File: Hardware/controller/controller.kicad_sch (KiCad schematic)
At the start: 48 parts, among them J101 Conn_02x10_Odd_Even, J102 Conn_02x10_Odd_Even, J103 Conn_02x10_Odd_Even, J104 Conn_02x08_Odd_Even, M101 Fan_4pin, Q101 MMBT3904, U101 PCA9543A, U102 EMC2101-R

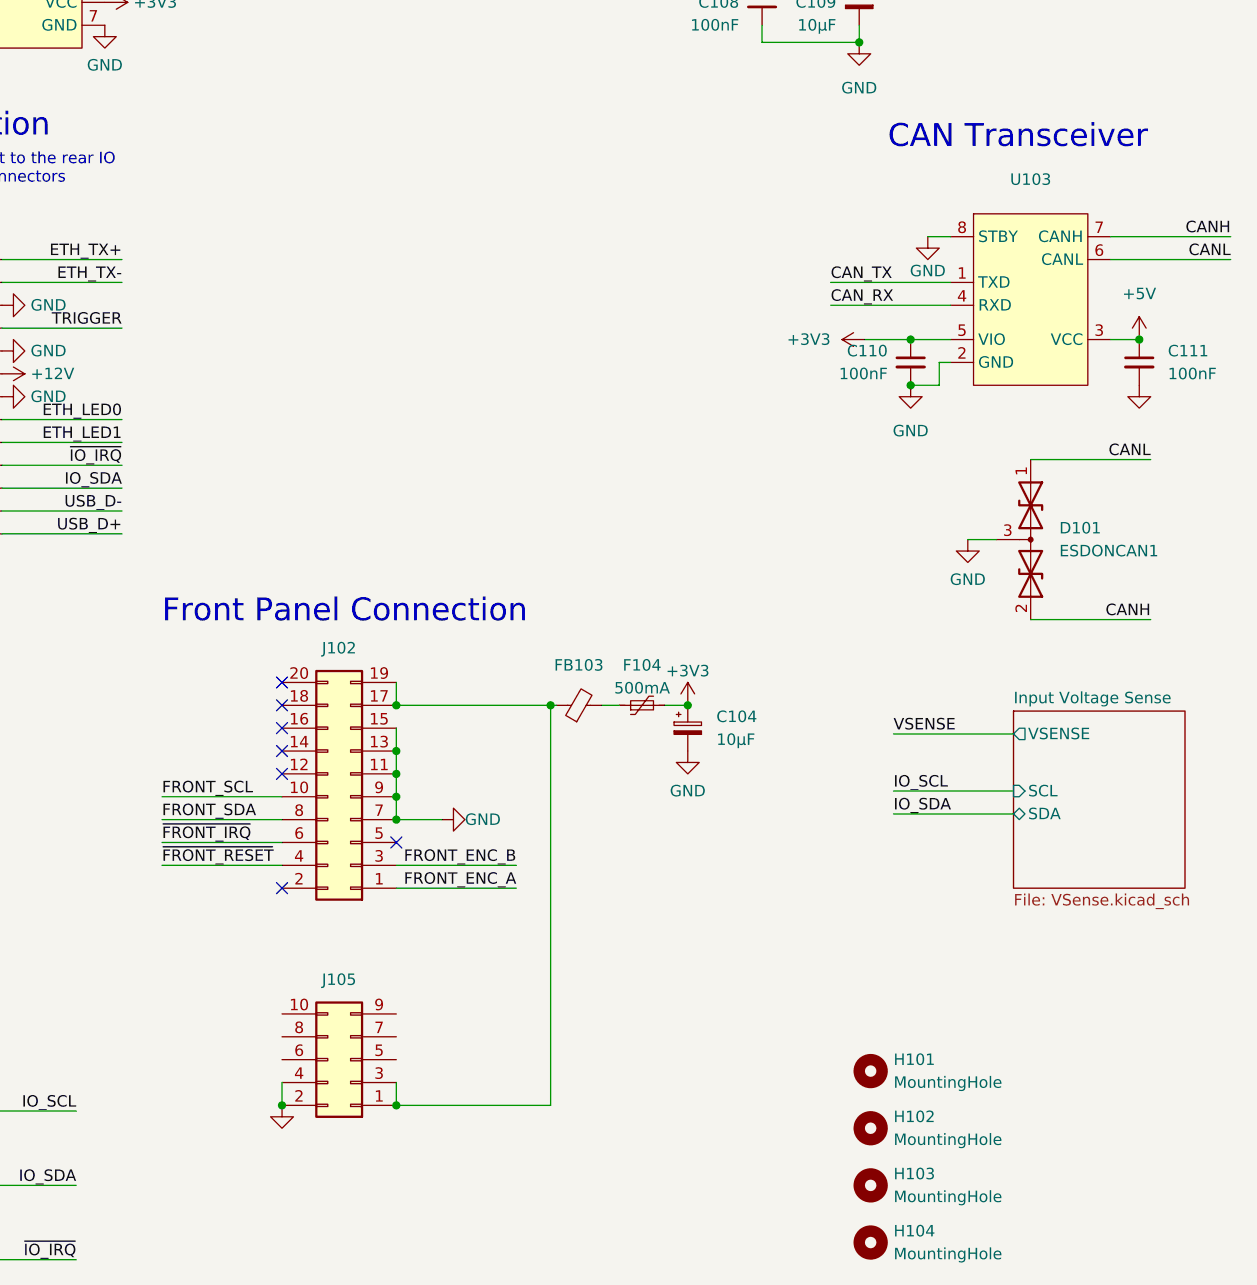
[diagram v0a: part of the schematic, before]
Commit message: Add "bonus display" board
- Created the bonus display board, which houses a chip-on-glass 4x10
  text character display. It's meant to be mounted next to the input
  jacks to show a constant location of current/voltage, even if the main
  display is used for menus or other stuff.

- More tweaks to controller board, to do with power generation and the
  front panel bonus display connector
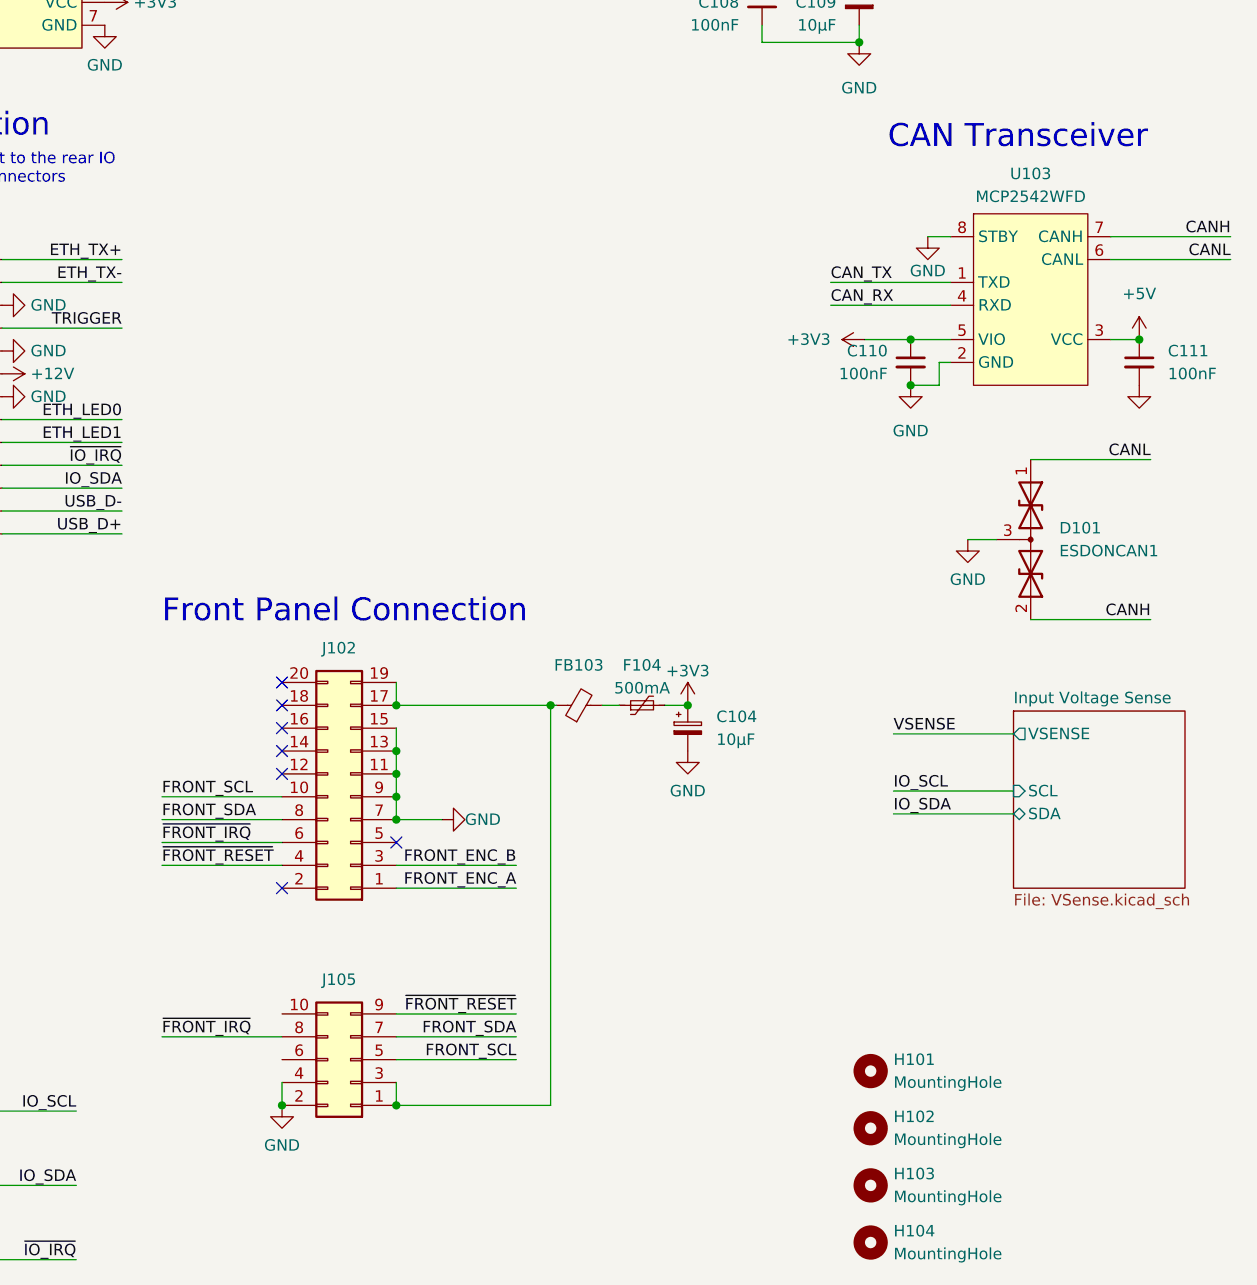
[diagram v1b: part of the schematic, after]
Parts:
- J105: value (none) -> Conn_02x05_Odd_Even; footprint (none) -> Connector_PinHeader_1.27mm:PinHeader_2x05_P1.27mm_Vertical_SMD
- U103: value (none) -> MCP2542WFD; footprint (none) -> Package_SO:SOIC-8_3.9x4.9mm_P1.27mm
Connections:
- net FRONT_SCL: now also J105.5 (Pin_5)
- net FRONT_SDA: now also J105.7 (Pin_7)
- net ~{FRONT_IRQ}: now also J105.8 (Pin_8)
- net ~{FRONT_RESET}: now also J105.9 (Pin_9)
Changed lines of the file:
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@@
+    (stroke (width 0) (type default) (color 0 0 0 0))
+  )
+  (wire (pts (xy 116.205 166.37) (xy 102.87 166.37))
     (stroke (width 0) (type default) (color 0 0 0 0))
   )
@@
     (stroke (width 0) (type default) (color 0 0 0 0))
   )
+  (wire (pts (xy 116.205 171.45) (xy 102.87 171.45))
+    (stroke (width 0) (type default) (color 0 0 0 0))
+  )
   (wire (pts (xy 186.69 104.775) (xy 173.355 104.775))
     (stroke (width 0) (type default) (color 0 0 0 0))
@@
     (stroke (width 0) (type default) (color 0 0 0 0))
   )
+  (wire (pts (xy 116.205 168.91) (xy 102.87 168.91))
+    (stroke (width 0) (type default) (color 0 0 0 0))
+  )
   (wire (pts (xy 76.835 147.32) (xy 90.17 147.32))
     (stroke (width 0) (type default) (color 0 0 0 0))
@@
   )
   (wire (pts (xy 46.355 185.42) (xy 46.355 177.165))
+    (stroke (width 0) (type default) (color 0 0 0 0))
+  )
+  (wire (pts (xy 76.835 168.91) (xy 90.17 168.91))
     (stroke (width 0) (type default) (color 0 0 0 0))
   )
@@
     (effects (font (size 1.27 1.27)) (justify left bottom))
   )
+  (label "FRONT_SDA" (at 116.205 168.91 180)
+    (effects (font (size 1.27 1.27)) (justify right bottom))
+  )
   (label "CAN_TX" (at 151.13 85.09 0)
     (effects (font (size 1.27 1.27)) (justify left bottom))
@@
     (effects (font (size 1.27 1.27)) (justify right bottom))
   )
+  (label "FRONT_SCL" (at 116.205 171.45 180)
+    (effects (font (size 1.27 1.27)) (justify right bottom))
+  )
   (label "ETH_TX+" (at 208.915 88.265 0)
     (effects (font (size 1.27 1.27)) (justify left bottom))
@@
     (effects (font (size 1.27 1.27)) (justify left bottom))
   )
+  (label "~{FRONT_IRQ}" (at 76.835 168.91 0)
+    (effects (font (size 1.27 1.27)) (justify left bottom))
+  )
   (label "IO_SCL" (at 67.31 177.165 180)
     (effects (font (size 1.27 1.27)) (justify right bottom))
@@
   (label "VSENSE" (at 208.915 114.935 0)
     (effects (font (size 1.27 1.27)) (justify left bottom))
+  )
+  (label "~{FRONT_RESET}" (at 116.205 166.37 180)
+    (effects (font (size 1.27 1.27)) (justify right bottom))
   )
   (symbol (lib_id "Device:D_TVS_Dual_AAC") (at 173.355 113.665 270) (unit 1)
@@
       (effects (font (size 1.27 1.27)) hide)
     )
-    (property "Value" "" (id 1) (at 90.17 180.975 0))
+    (property "Value" "GND" (id 1) (at 90.17 180.975 0))
     (property "Footprint" "" (id 2) (at 90.17 176.53 0)
       (effects (font (size 1.27 1.27)) hide)
@@
   (symbol (lib_id "programmable-load:MCP2542WFD") (at 173.355 85.09 0) (unit 1)
     (in_bom yes) (on_board yes)
-    (property "Reference" "U103" (id 0) (at 173.355 73.66 0))
-    (property "Value" "" (id 1) (at 173.355 76.2 0))
-    (property "Footprint" "" (id 2) (at 173.355 97.79 0)
+    (property "Reference" "U103" (id 0) (at 173.355 73.025 0))
+    (property "Value" "MCP2542WFD" (id 1) (at 173.355 75.565 0))
+    (property "Footprint" "Package_SO:SOIC-8_3.9x4.9mm_P1.27mm" (id 2) (at 173.355 97.79 0)
       (effects (font (size 1.27 1.27) italic) hide)
     )
@@
     (in_bom yes) (on_board yes)
     (property "Reference" "J105" (id 0) (at 96.52 162.56 0))
-    (property "Value" "" (id 1) (at 96.52 161.925 0)
-      (effects (font (size 1.27 1.27)) hide)
-    )
-    (property "Footprint" "" (id 2) (at 97.79 171.45 0)
-      (effects (font (size 1.27 1.27)) hide)
-    )
+    (property "Value" "Conn_02x05_Odd_Even" (id 1) (at 96.52 161.925 0)
+      (effects (font (size 1.27 1.27)) hide)
+    )
+    (property "Footprint" "Connector_PinHeader_1.27mm:PinHeader_2x05_P1.27mm_Vertical_SMD" (id 2) (at 97.79 171.45 0)
+      (effects (font (size 1.27 1.27)) hide)
+    )

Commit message: Refactoring controller schematic
- Moved most of the connections out of the main sheet and into
  appropriate subsheets to increase the organization

- Updated analog board connection to have the SPI bus concept rather
  than a CAN bus; that way we don't need an additional micro on the
  analog board to drive things also

- Replaced latching connectors with regular shrouded headers
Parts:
- removed C103, C104, C109: 10µF, Capacitor_Tantalum_SMD:CP_EIA-3216-18_Kemet-A_Pad1.58x1.35mm_HandSolder, symbol Device:C_Polarized_Small
- removed C106, C108, C110, C111: 100nF, Capacitor_SMD:C_0805_2012Metric_Pad1.18x1.45mm_HandSolder, symbol Device:C_Small
- removed D101: ESDONCAN1, Package_TO_SOT_SMD:SOT-23_Handsoldering, symbol Device:D_TVS_Dual_AAC
- removed F103: 250mA, Fuse:Fuse_1206_3216Metric_Pad1.42x1.75mm_HandSolder, symbol Device:Polyfuse_Small
- removed F104, F105: 500mA, Fuse:Fuse_1206_3216Metric_Pad1.42x1.75mm_HandSolder, symbol Device:Polyfuse_Small
- removed FB101, FB103: FerriteBead_Small, Inductor_SMD:L_0805_2012Metric_Pad1.05x1.20mm_HandSolder, symbol Device:FerriteBead_Small
- removed J102: Conn_02x10_Odd_Even, Connector_PinHeader_1.27mm:PinHeader_2x10_P1.27mm_Vertical_SMD, symbol Connector_Generic:Conn_02x10_Odd_Even
- removed J103: Conn_02x10_Odd_Even, Connector_PinHeader_1.27mm:PinHeader_2x13_P1.27mm_Vertical, symbol Connector_Generic:Conn_02x13_Odd_Even
- removed J104: Conn_02x08_Odd_Even, Connector_IDC:IDC-Header_2x08-1MP_P2.54mm_Latch_Horizontal, symbol Connector_Generic:Conn_02x08_Odd_Even
- removed J105: Conn_02x05_Odd_Even, Connector_PinHeader_1.27mm:PinHeader_2x05_P1.27mm_Vertical_SMD, symbol Connector_Generic:Conn_02x05_Odd_Even
- removed R103, R104, R105, R106: 2k2, Resistor_SMD:R_0805_2012Metric_Pad1.20x1.40mm_HandSolder, symbol Device:R_Small
- removed R107, R108, R109, R111, R112: 10k, Resistor_SMD:R_0805_2012Metric_Pad1.20x1.40mm_HandSolder, symbol Device:R_Small
- removed U102: EMC2101-R, Package_SO:MSOP-8_3x3mm_P0.65mm, symbol programmable-load:EMC2101-R
- removed U103: MCP2542WFD, Package_SO:SOIC-8_3.9x4.9mm_P1.27mm, symbol programmable-load:MCP2542WFD
- J101: footprint Connector_IDC:IDC-Header_2x05-1MP_P2.54mm_Latch_Horizontal -> Connector_IDC:IDC-Header_2x10_P2.54mm_Horizontal; symbol Connector_Generic:Conn_02x05_Odd_Even -> Connector_Generic:Conn_02x10_Odd_Even; MPN 61201022121 -> 61202021721
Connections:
- net +3V3: now also J101.13 (Pin_13), J101.15 (Pin_15)
- net GND: now also J101.7 (Pin_7); no longer J101.10 (Pin_10), J101.2 (Pin_2), J101.4 (Pin_4), J101.6 (Pin_6), J101.8 (Pin_8)
- net CANH renamed ANA_MISO
- net CANL renamed ANA_SEL0
- new net: J101.14 (Pin_14), J101.16 (Pin_16), J101.18 (Pin_18), J101.20 (Pin_20)
- new net: FB102.1, J101.17 (Pin_17), J101.19 (Pin_19)
- new net ANA_MOSI: J101.6 (Pin_6)
- new net ANA_SCK: J101.5 (Pin_5)
- new net ANA_SEL1: J101.2 (Pin_2)
- new net ~{ANA_CS}: J101.4 (Pin_4)
- new net ~{ANA_IRQ}: J101.8 (Pin_8)
- new net ~{ANA_RESET}: J101.9 (Pin_9)
- no-connect marks 11 -> 0
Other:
- added sheet Front Panel Connections (io-front.kicad_sch)
- added sheet Rear IO Connections (io-rear.kicad_sch)
- sheet CPU ports: added ANALOG_MISO, ANALOG_MOSI, ANALOG_SCK, ANALOG_SEL0, ANALOG_SEL1, FAN_PWM, ~{ANALOG_CS}, ~{ANALOG_IRQ}, ~{ANALOG_RESET}; removed ~{DRIVER_IRQ}, ~{DRIVER_RESET}
- note added: "*** TODO: fuse for +3V3"
- note added: "Analog Board Connection"
- note added: "Connect to internal load boards Provides to loads: +12V, +3V3"
- note removed: "CAN Transceiver"
- note removed: "Connect to internal load boards Provides to loads: +12V, +5V, +3V3"
- note removed: "Driver Board Connection"
- note removed: "Front Panel Connection"
- note removed: "Host loads regs, fan at 0%"
- note removed: "I²C address: 0b1001100"
- note removed: "Provide USB, I²C, CAN, Ethernet to the rear IO board, which has the actual connectors"
- note removed: "Rear IO connection"
- note removed: "To OLED"
- moved on the sheet: C101, C102, F101, FB102, R117, R118, U101

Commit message: More tweaks to controller layout
- Wired up the fan connector to work with PWM control, directly from one
  of the processor's timer/counter's signal generator outputs. For now
  the tachometer output is ignored, but we might do something with it
  later

- Moved around a few passives
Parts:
- removed C107: 10µF, Capacitor_THT:CP_Radial_D5.0mm_P2.00mm, symbol Device:C_Polarized_Small
- removed M101: Fan_4pin, programmable-load:Molex-47053-1000-MFG, symbol Motor:Fan_4pin
- removed Q101: MMBT3904, Package_TO_SOT_SMD:SOT-323_SC-70_Handsoldering, symbol Transistor_BJT:MMBT3904
- removed R113, R116: 4k7, Resistor_SMD:R_0805_2012Metric_Pad1.20x1.40mm_HandSolder, symbol Device:R_Small
- removed R114: 10k, Resistor_SMD:R_0805_2012Metric_Pad1.20x1.40mm_HandSolder, symbol Device:R_Small
- removed R115: 27k4, Resistor_SMD:R_0805_2012Metric_Pad1.20x1.40mm_HandSolder, symbol Device:R_Small
- added F102: 500mA, Fuse:Fuse_1206_3216Metric_Pad1.42x1.75mm_HandSolder, symbol Device:Polyfuse_Small
- added R101, R102: 2k2, Resistor_SMD:R_0805_2012Metric_Pad1.20x1.40mm_HandSolder, symbol Device:R_Small
- added R103: (no value), symbol Device:R_Small
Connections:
- net +3V3: now also F102.1, R101.2, R102.2, R103.2; no longer J101.13 (Pin_13), J101.15 (Pin_15)
- net ANA_SCL: now also J101.11 (Pin_11), R101.1
- net ANA_SDA: now also J101.10 (Pin_10), R102.1
- net GND: now also J101.13 (Pin_13), J101.15 (Pin_15), J101.18 (Pin_18), J101.20 (Pin_20)
- net ~{ANA_IRQ}: now also R103.1
- net at J101.14 (Pin_14), J101.16 (Pin_16): now also F102.2; no longer J101.18 (Pin_18), J101.20 (Pin_20)
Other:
- sheet CPU ports: added ANALOG_SCL, ANALOG_SDA; removed DRIVER_SCL, DRIVER_SDA
- sheet Rear IO Connections ports: added FAN_PWM; removed none
- note removed: "A 4-pin PWM fan mounted to the rear panel of the case is used to exhaust hot air"
- note removed: "Rear Panel Fan Controller"

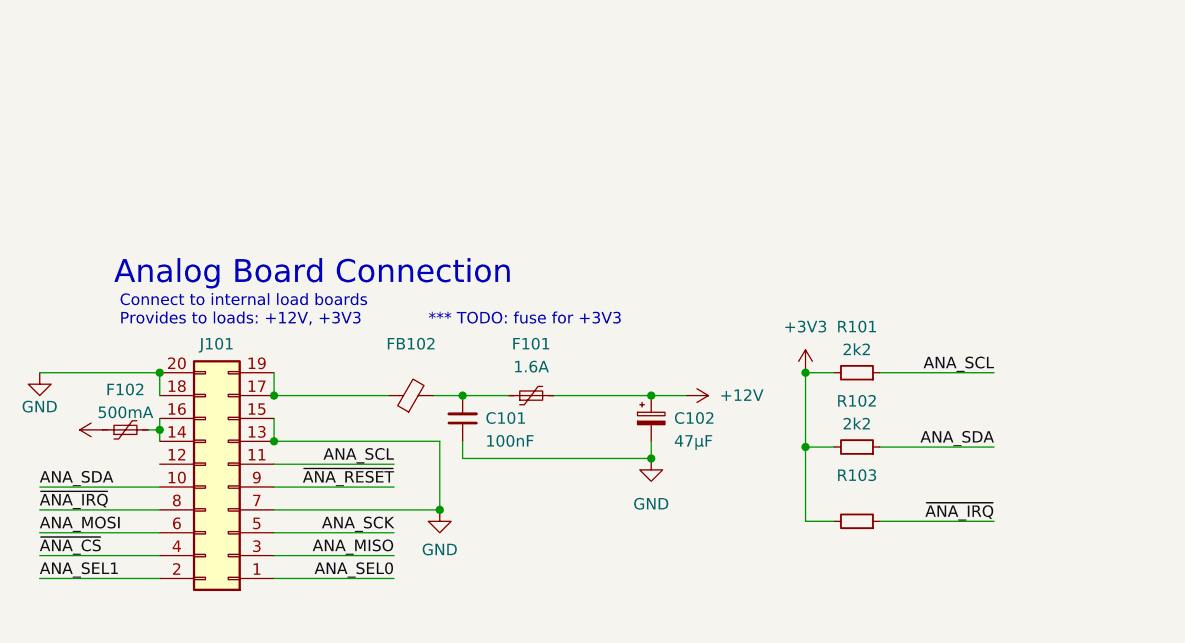
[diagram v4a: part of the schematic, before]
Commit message: Changed analog board connector pinout
- Changed the pinout of the power rails on the analog board to be more
  convenient for the analog board

- Tweaked a few more existing footprints and added some symbols
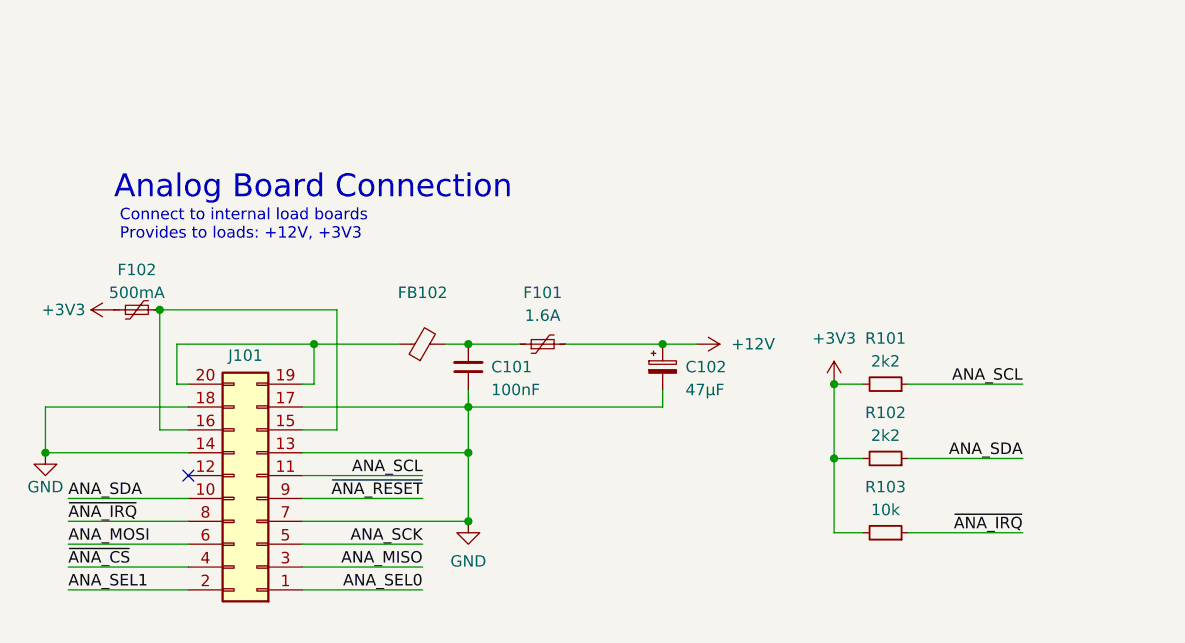
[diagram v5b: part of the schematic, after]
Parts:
- R103: value (none) -> 10k; footprint (none) -> Resistor_SMD:R_0805_2012Metric_Pad1.20x1.40mm_HandSolder
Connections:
- net GND: now also J101.14 (Pin_14), J101.17 (Pin_17); no longer J101.15 (Pin_15), J101.20 (Pin_20)
- net at F102.2, J101.16 (Pin_16): now also J101.15 (Pin_15); no longer J101.14 (Pin_14)
- net at FB102.1, J101.19 (Pin_19): now also J101.20 (Pin_20); no longer J101.17 (Pin_17)
- no-connect marks 0 -> 1
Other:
- note removed: "*** TODO: fuse for +3V3"
- moved on the sheet: C101, C102, F101, F102, FB102, J101, R101, R102, R103
